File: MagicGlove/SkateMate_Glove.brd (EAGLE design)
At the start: 43 x 27 mm, 42 parts, among them IC1 BU33TD3WG, IC2 LMV321M5, U2 ATMEGA328PB-AU

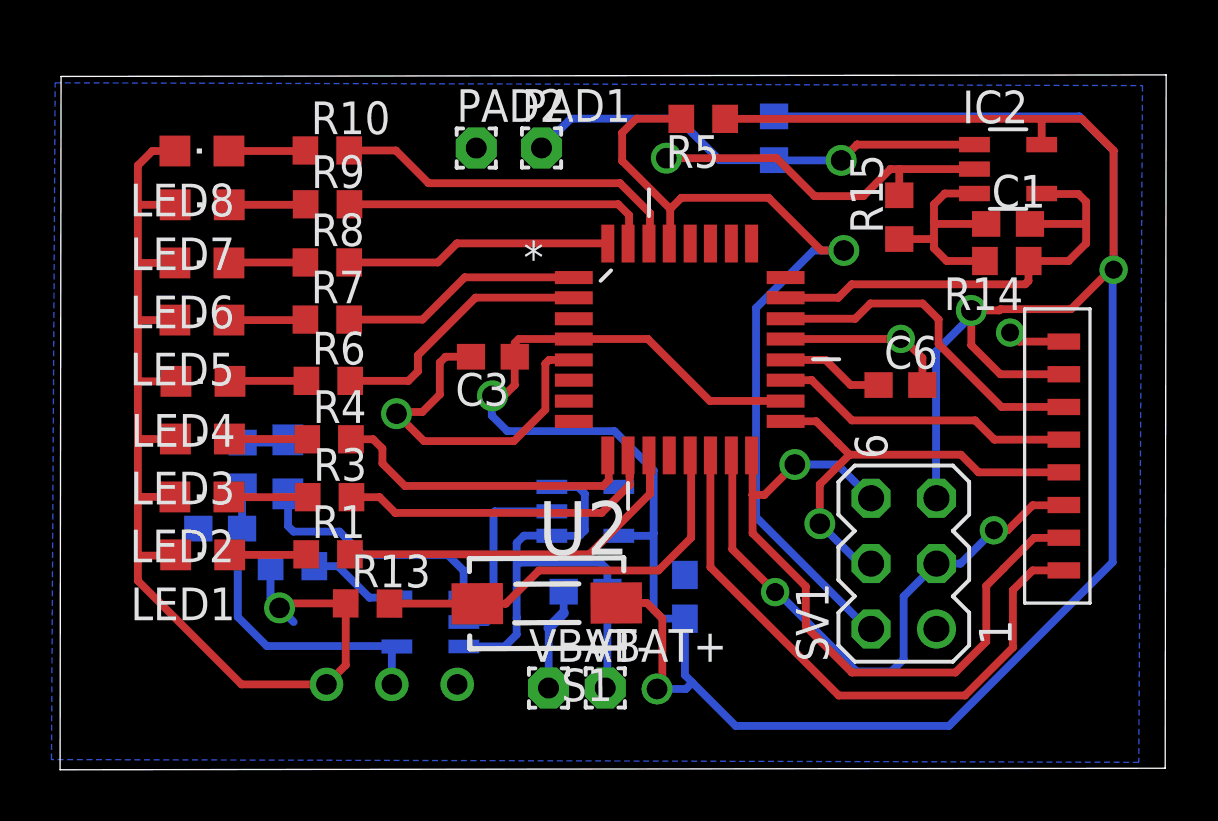
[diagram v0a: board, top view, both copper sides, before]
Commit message: New Version of MagicGlove Print 	- Rewired the analog part 	- Smaller Layout alltogether Initial Version of MagicGlove Receiver Print 	- Some GPIO Pads for anything that might be added
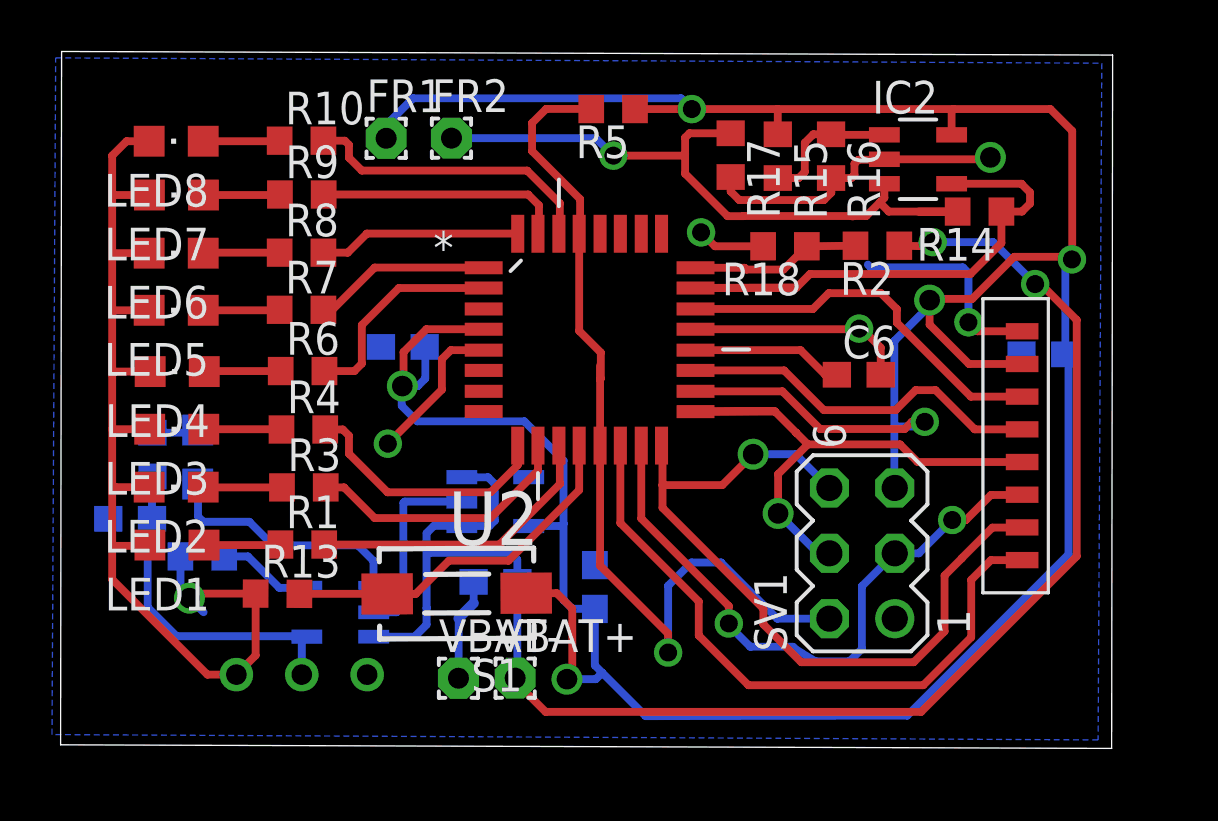
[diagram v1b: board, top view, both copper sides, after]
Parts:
- removed PAD1: -, wirepad:1,6/0,8
- removed PAD2: +, wirepad:1,6/0,8
- added FR1: +, wirepad:1,6/0,8
- added FR2: -, wirepad:1,6/0,8
- added R16, R17, R18: 13k, eagle-ltspice:R0603
- C1: value .47u -> 100n
- R1, R10, R3, R4, R6, R7, R8, R9: value 150 -> 82
- R11: value 2k -> 62k
- R14: value 10k -> 24k
- R15: value 10k -> 18k
- R2: value 10k -> 13k
- moved R2 5.79 mm to (31.7, 19.4), flipped to the top, turned to 180 degrees
- moved R15 5.28 mm to (27.9, 22.9), turned to 270 degrees
- moved C1 5.25 mm to (38.2, 15.2), flipped to the bottom
- moved C3 3.52 mm to (13.3, 15.4), flipped to the bottom, turned to 0 degrees
- moved C7 3.52 mm to (20.8, 6.12)
- moved C8 3.52 mm to (16.9, 6.32)
- moved LED9 3.52 mm to (5.32, 11.2)
- moved R12 3.52 mm to (3.57, 11.3)
- moved R13 3.52 mm to (8.42, 5.86)
- moved R5 3.52 mm to (21.5, 24.7)
- moved S1 3.52 mm to (15.4, 5.87)
- moved U$1 3.52 mm to (10.9, 5.14)
- moved U$3 3.52 mm to (9.37, 2.72)
- moved U2 3.52 mm to (20.6, 15.7)
- moved VBAT+ 3.52 mm to (17.7, 2.58)
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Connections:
- removed net N$14: C1.2, IC2.4, R14.1, U2.23
- removed net N$21: C8.1, IC1.1, IC1.3, U$1.3, VBAT+.1
- removed net N$26: IC2.1, PAD1.1, R2.2
- removed net N$5: C1.1, IC2.3, R14.2, R15.1
- new net ADIN: IC2.4, R14.1, U2.23
- new net ADVBAT: R18.1, R2.2, U2.24
- new net DMSREF+: IC2.1, R15.2, R16.1
- new net DMSREF-: FR2.1, IC2.3, R14.2, R17.1
- new net VBAT+: C8.1, IC1.1, IC1.3, R2.1, U$1.3, VBAT+.1
- net +3V3: now also C1.1, FR1.1, R15.1; no longer R2.1
- net GND: now also C1.2, R16.2, R17.2, R18.2; no longer PAD2.1, R15.2
- net N$3: now also U2.12; no longer U2.13
- net RESETICSP: now also U2.13
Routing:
- net VBAT+: track 0.00 -> 62.2 mm, vias 0 -> 2
- net DMSREF-: track 0.00 -> 26.8 mm, vias 0 -> 1
- net ADIN: track 0.00 -> 22.6 mm
- net N$21: track 19.8 -> 0.00 mm
- net N$14: track 19.0 -> 0.00 mm
- net N$26: track 18.3 -> 0.00 mm, vias 1 -> 0
- net N$5: track 9.08 -> 0.00 mm
- net ADVBAT: track 0.00 -> 6.62 mm
- net DMSREF+: track 0.00 -> 6.05 mm
- net SCK: track 17.4 -> 22.4 mm
- net +3V3: track 129.4 -> 132.8 mm, vias 4 -> 6
- net N$13: track 13.5 -> 10.5 mm
- net MISO: track 27.6 -> 30.5 mm
- net CSN: track 11.8 -> 14.3 mm
- net N$17: track 9.42 -> 6.92 mm
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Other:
- board size 43 x 27 mm -> 40.9 x 27.1 mm

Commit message: Receiver Board v1.0 working
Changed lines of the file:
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@@
 <wire x1="21.04" y1="2.79" x2="22.725703125" y2="1.104296875" width="0.3048" layer="16"/>
 <wire x1="21.04" y1="2.79" x2="20.7525" y2="3.0775" width="0.3048" layer="16"/>
-<wire x1="32.39" y1="9.9855" x2="32.39" y2="15.68" width="0.3048" layer="16"/>
-<wire x1="32.39" y1="9.9855" x2="32.4055" y2="9.97" width="0.3048" layer="16"/>
+<wire x1="32.39" y1="12.36" x2="32.39" y2="15.68" width="0.3048" layer="16"/>
 <wire x1="33.7591" y1="17.2673" x2="33.7591" y2="16.315" width="0.3048" layer="1"/>
 <wire x1="33.7591" y1="17.0491" x2="33.7591" y2="17.2673" width="0.3048" layer="16"/>
@@
 <wire x1="14.165" y1="14.22" x2="14.165" y2="15.4237" width="0.3048" layer="16"/>
 <wire x1="14.165" y1="15.4237" x2="14.1415" y2="15.4472" width="0.3048" layer="16"/>
-<wire x1="32.4055" y1="9.97" x2="32.79" y2="12.26" width="0" layer="19" extent="1-1"/>
+<wire x1="32.39" y1="9.97" x2="32.4055" y2="9.97" width="0.4064" layer="16"/>
+<wire x1="32.4055" y1="9.97" x2="32.39" y2="9.97" width="0.3048" layer="16"/>
+<wire x1="32.39" y1="9.97" x2="32.39" y2="12.36" width="0.3048" layer="16"/>
 </signal>
 <signal name="RESETICSP">

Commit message: style
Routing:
- net N$5: track 3.73 -> 0.00 mm
- net N$24: track 13.4 -> 11.5 mm
- net VBAT+: track 62.2 -> 60.6 mm
- net GND: track 92.7 -> 91.9 mm
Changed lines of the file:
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@@
 <?xml version="1.0" encoding="utf-8"?>
 <!DOCTYPE eagle SYSTEM "eagle.dtd">
-<eagle version="8.1.0">
+<eagle version="7.6.0">
 <drawing>
 <settings>
@@
 <contactref element="C9" pad="2"/>
 <contactref element="R11" pad="2"/>
-<contactref element="U$1" pad="2"/>
 <contactref element="VBAT-" pad="1"/>
 <polygon width="0.3048" layer="16" spacing="0.254" isolate="0.6096">
@@
 <wire x1="13.366" y1="9.44" x2="15.5824" y2="9.44" width="0.3048" layer="16"/>
 <wire x1="13.366" y1="9.44" x2="13.3145" y2="9.3885" width="0.3048" layer="16"/>
-<wire x1="12.1625" y1="5.14" x2="13.0535" y2="5.14" width="0.3048" layer="16"/>
 <wire x1="13.0535" y1="5.14" x2="13.3145" y2="5.401" width="0.3048" layer="16"/>
 <wire x1="13.3145" y1="5.401" x2="13.3145" y2="9.3885" width="0.3048" layer="16"/>
@@
 <wire x1="2" y1="6.4175" x2="5.7" y2="2.7175" width="0.3048" layer="1"/>
 <wire x1="2" y1="7.72" x2="2" y2="6.4175" width="0.3048" layer="1"/>
-<wire x1="3.4365" y1="7.72" x2="3.4675" y2="7.751" width="0" layer="19" extent="1-1"/>
+<contactref element="U$1" pad="2"/>
+<wire x1="37.33" y1="15.16" x2="37.3537" y2="16.0566" width="0" layer="19" extent="1-16"/>
+<wire x1="31.12" y1="16.16" x2="31.47" y2="18.54" width="0" layer="19" extent="1-16"/>
+<wire x1="29.6544" y1="21.1544" x2="31.36" y2="18.65" width="0" layer="19" extent="1-16"/>
+<wire x1="24.88" y1="19.9" x2="26.3656" y2="21.1544" width="0" layer="19" extent="1-1"/>
+<wire x1="16.4352" y1="15.3236" x2="24.6648" y2="16.1364" width="0" layer="19" extent="1-1"/>
+<wire x1="13.366" y1="9.44" x2="12.71" y2="11.69" width="0" layer="19" extent="1-16"/>
+<wire x1="12.1625" y1="5.14" x2="13.0535" y2="5.14" width="0" layer="19" extent="16-16"/>
+<wire x1="15.46" y1="4.91" x2="13.3145" y2="5.401" width="0" layer="19" extent="16-16"/>
+<wire x1="12.4415" y1="15.4472" x2="14.81" y2="14.975" width="0" layer="19" extent="1-16"/>
+<wire x1="11.906" y1="2.7175" x2="12.1625" y2="5.14" width="0" layer="19" extent="16-16"/>
+<wire x1="7.574209375" y1="3.465709375" x2="11.906" y2="2.7175" width="0" layer="19" extent="1-1"/>
+<wire x1="3.4675" y1="7.751" x2="3.4365" y2="7.72" width="0" layer="19" extent="1-1"/>
+<wire x1="1.8465" y1="8.7701" x2="2" y2="7.72" width="0" layer="19" extent="1-16"/>
+<wire x1="20.7525" y1="6.97" x2="16.0425" y2="6.32" width="0" layer="19" extent="16-16"/>
+<wire x1="32.4055" y1="4.89" x2="31.856" y2="14.368" width="0" layer="19" extent="1-1"/>
 </signal>
 <signal name="+3V3">
@@
 <contactref element="C8" pad="1"/>
 <contactref element="IC1" pad="3"/>
-<contactref element="U$1" pad="3"/>
 <contactref element="VBAT+" pad="1"/>
 <wire x1="14.3225" y1="7.45" x2="14.3325" y2="7.44" width="0.3048" layer="16"/>
 <wire x1="15.5789" y1="8.4865" x2="15.5824" y2="8.49" width="0.3048" layer="16"/>
-<wire x1="12.17" y1="4.1975" x2="12.1625" y2="4.19" width="0.3048" layer="16"/>
-<wire x1="12.1625" y1="4.19" x2="13.7485" y2="4.19" width="0.3048" layer="16"/>
 <wire x1="13.7485" y1="4.19" x2="14.2155" y2="4.657" width="0.3048" layer="16"/>
 <wire x1="14.2155" y1="4.657" x2="14.2155" y2="5.313" width="0.3048" layer="16"/>
@@
 <wire x1="37.86" y1="17.89" x2="38.08" y2="17.89" width="0.3048" layer="1"/>
 <wire x1="38.08" y1="17.89" x2="39.473628125" y2="16.496371875" width="0.3048" layer="1"/>
+<contactref element="U$1" pad="3"/>
+<wire x1="12.1625" y1="4.19" x2="13.7485" y2="4.19" width="0" layer="19" extent="16-16"/>
 </signal>
 <signal name="N$22">
@@
 <contactref element="U$1" pad="4"/>
 <contactref element="R12" pad="1"/>
-<contactref element="C9" pad="1"/>
 <contactref element="U$3" pad="P$1"/>
 <wire x1="9.366" y1="2.7175" x2="9.366" y2="3.9935" width="0.3048" layer="16"/>
@@
 <wire x1="9.544" y1="4.2085" x2="9.5625" y2="4.19" width="0.3048" layer="16"/>
 <wire x1="3.38" y1="5.3345" x2="3.38" y2="8.6036" width="0.3048" layer="16"/>
-<wire x1="3.38" y1="8.6036" x2="3.5465" y2="8.7701" width="0.3048" layer="16"/>
-<wire x1="3.5465" y1="8.7701" x2="3.5465" y2="10.3948" width="0.3048" layer="16"/>
 <wire x1="3.5465" y1="10.3948" x2="3.566" y2="10.4143" width="0.3048" layer="16"/>
-</signal>
-<signal name="N$25">
-<contactref element="U$1" pad="5"/>
-<contactref element="R11" pad="1"/>
-<wire x1="9.5625" y1="6.09" x2="9.5525" y2="6.1" width="0.3048" layer="16"/>
-<wire x1="6.3525" y1="7.31" x2="7.273" y2="7.31" width="0.3048" layer="16"/>
-<wire x1="7.273" y1="7.31" x2="8.496" y2="6.087" width="0.3048" layer="16"/>
-<wire x1="8.496" y1="6.087" x2="9.5595" y2="6.087" width="0.3048" layer="16"/>
-<wire x1="9.5595" y1="6.087" x2="9.5625" y2="6.09" width="0.3048" layer="16"/>
+<contactref element="C9" pad="1"/>
+<wire x1="3.5465" y1="8.7701" x2="3.5465" y2="10.3948" width="0" layer="19" extent="16-16"/>
+<wire x1="3.38" y1="8.6036" x2="3.5465" y2="8.7701" width="0" layer="19" extent="16-16"/>
 </signal>
 <signal name="N$3">
@@
 <wire x1="28.0844" y1="18.4544" x2="28.99" y2="19.36" width="0.3048" layer="1"/>
 </signal>
+<signal name="N$5">
+<contactref element="U$1" pad="5"/>
+<contactref element="R11" pad="1"/>
+<wire x1="6.3525" y1="7.31" x2="9.5625" y2="6.09" width="0" layer="19" extent="16-16"/>
+</signal>
 </signals>
